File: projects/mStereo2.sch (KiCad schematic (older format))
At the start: 27 parts, among them P101 CONN_AMANERO, P102 MOLEX KK 1x2, P103 MOLEX KK 1X3, P104 XLR-MALE, P105 XLR-MALE, U101 ISO7640, U102 CDCLVC1104, U103 MCP100-315DI, U104 SRC4192, X101 XTAL

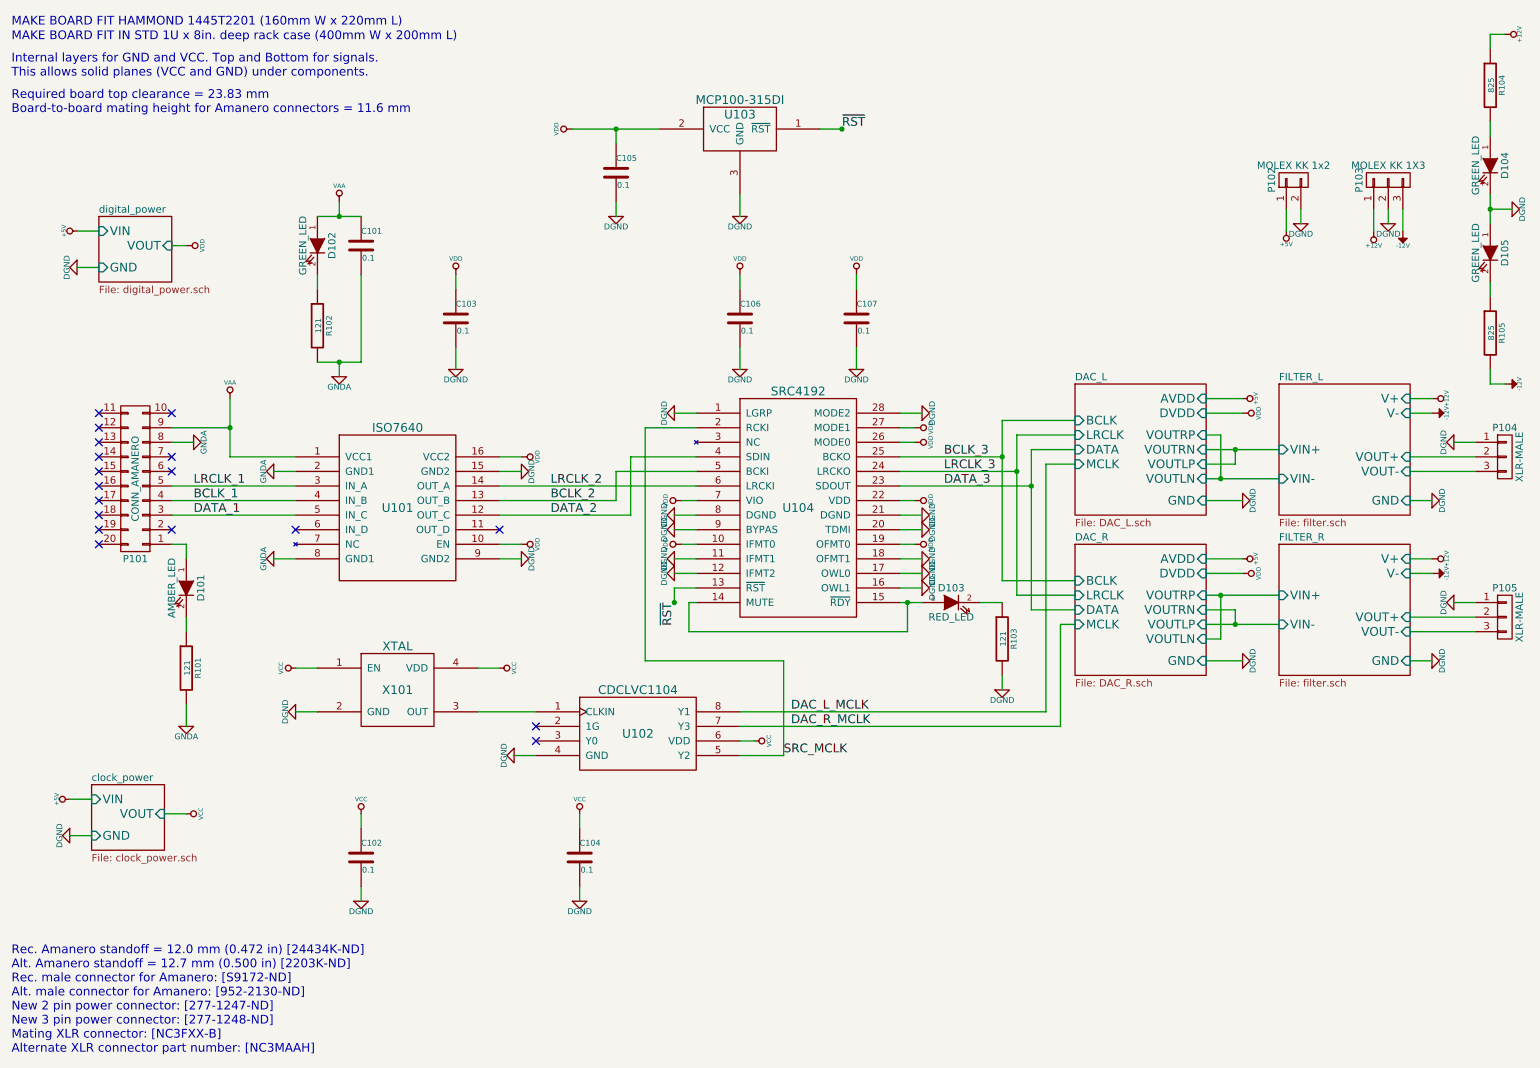
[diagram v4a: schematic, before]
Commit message: add connector footprints; change c_pol sch symbols
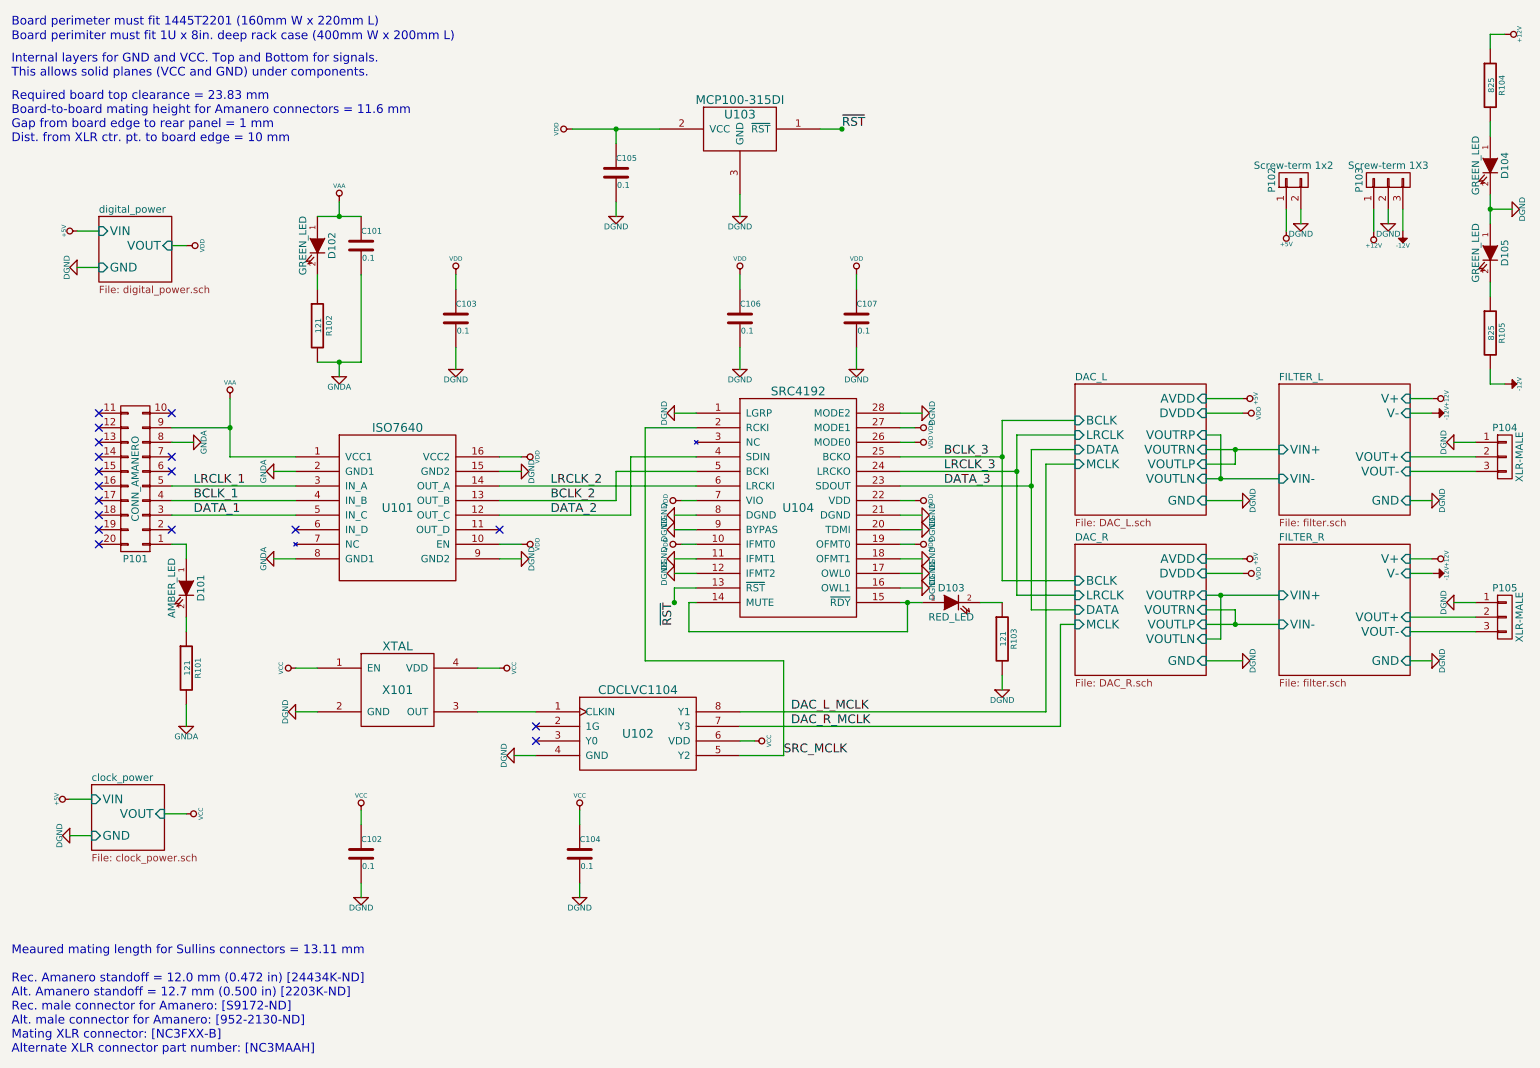
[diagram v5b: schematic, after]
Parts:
- P102: value MOLEX KK 1x2 -> Screw-term 1x2; Description (none) -> CONN TERM BLOCK 2POS 5.08MM PCB; Manu Molex -> Phoenix Contact; Manu-PN 0022232021 -> 1729128; Supplier-PN WM4200-ND -> 277-1247-ND
- P103: value MOLEX KK 1X3 -> Screw-term 1X3; Description (none) -> CONN TERM BLOCK 3POS 5.08MM PCB; Manu Molex -> Phoenix Contact; Manu-PN 0022232031 -> 1729131; Supplier-PN WM4201-ND -> 77-1248-ND
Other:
- note added: "Board perimeter must fit 1445T2201 (160mm W x 220mm L)"
- note added: "Board perimiter must fit 1U x 8in. deep rack case (400mm W x 200mm L)"
- note added: "Meaured mating length for Sullins connectors = 13.11 mm\n\nRec. Amanero standoff = 12.0 mm (0.472 in) [24434K-ND]\nAlt. Amanero standoff = 12.7 mm (0.500 in) [2203K-ND]\nRec. male connector for Amanero: [S9172-ND]\nAlt. male connector for Amanero: [952-2130-ND]\nMating XLR connector: [NC3FXX-B]\nAlternate XLR connector part number: [NC3MAAH]\n"
- note added: "Required board top clearance = 23.83 mm\nBoard-to-board mating height for Amanero connectors = 11.6 mm\nGap from board edge to rear panel = 1 mm\nDist. from XLR ctr. pt. to board edge = 10 mm\n"
- note removed: "MAKE BOARD FIT HAMMOND 1445T2201 (160mm W x 220mm L)"
- note removed: "MAKE BOARD FIT IN STD 1U x 8in. deep rack case (400mm W x 200mm L)"
- note removed: "Rec. Amanero standoff = 12.0 mm (0.472 in) [24434K-ND]\nAlt. Amanero standoff = 12.7 mm (0.500 in) [2203K-ND]\nRec. male connector for Amanero: [S9172-ND]\nAlt. male connector for Amanero: [952-2130-ND]\nNew 2 pin power connector: [277-1247-ND]\nNew 3 pin power connector: [277-1248-ND]\nMating XLR connector: [NC3FXX-B]\nAlternate XLR connector part number: [NC3MAAH]\n"
- note removed: "Required board top clearance = 23.83 mm\nBoard-to-board mating height for Amanero connectors = 11.6 mm\n"
- moved on the sheet: C102, C104

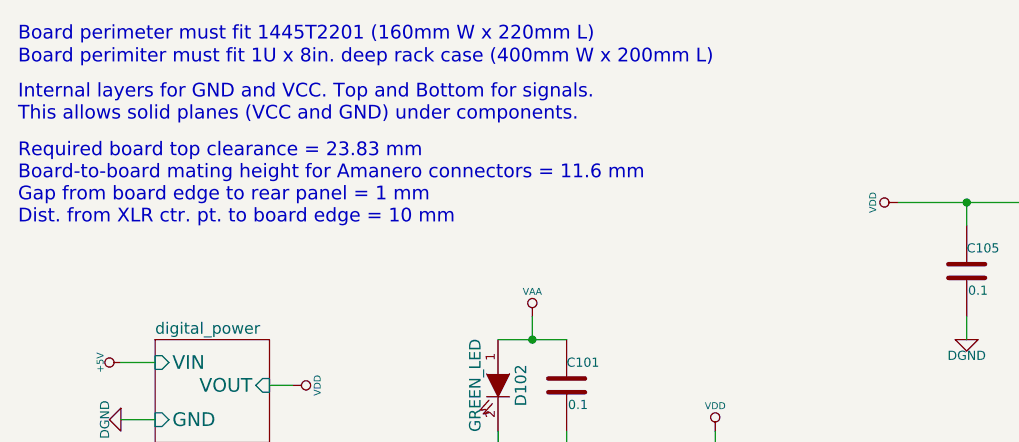
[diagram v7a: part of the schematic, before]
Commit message: prelimiary component positioning, board resizing, added mounting holes footprint
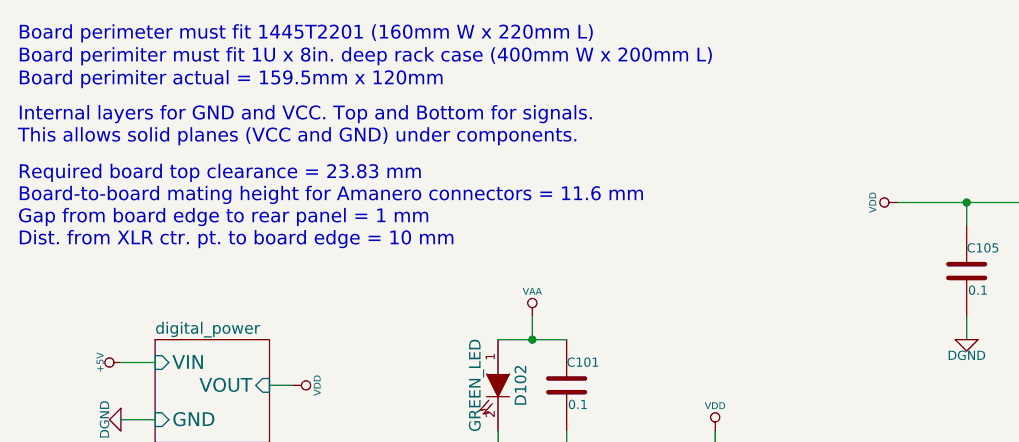
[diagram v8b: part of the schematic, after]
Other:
- note added: "Board perimiter actual = 159.5mm x 120mm"
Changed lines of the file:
@@
 LIBS:led_gosselin
 LIBS:wolfson_gosselin
-LIBS:mStereo2-cache
 EELAYER 24 0
 EELAYER END
@@
 Text Notes 550  750  0    60   ~ 0
 Board perimiter must fit 1U x 8in. deep rack case (400mm W x 200mm L)
-Text Notes 550  1000 0    60   ~ 0
+Text Notes 550  1100 0    60   ~ 0
 Internal layers for GND and VCC. Top and Bottom for signals.\nThis allows solid planes (VCC and GND) under components.
 $Comp
@@
 Text Notes 550  7700 0    60   ~ 0
 Meaured mating length for Sullins connectors = 13.11 mm\n\nRec. Amanero standoff = 12.0 mm (0.472 in) [24434K-ND]\nAlt. Amanero standoff = 12.7 mm (0.500 in) [2203K-ND]\nRec. male connector for Amanero: [S9172-ND]\nAlt. male connector for Amanero: [952-2130-ND]\nMating XLR connector: [NC3FXX-B]\nAlternate XLR connector part number: [NC3MAAH]\n
-Text Notes 550  1450 0    60   ~ 0
+Text Notes 550  1550 0    60   ~ 0
 Required board top clearance = 23.83 mm\nBoard-to-board mating height for Amanero connectors = 11.6 mm\nGap from board edge to rear panel = 1 mm\nDist. from XLR ctr. pt. to board edge = 10 mm\n
+Text Notes 550  850  0    60   ~ 0
+Board perimiter actual = 159.5mm x 120mm
 $EndSCHEMATC
